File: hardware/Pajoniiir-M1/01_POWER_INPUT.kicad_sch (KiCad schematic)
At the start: 0 parts

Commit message: hardware: capture Rev A input eFuse schematic
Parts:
- added C1, C6: 100nF, Capacitor_SMD:C_0603_1608Metric, symbol Device:C
- added C2: 10uF, Capacitor_SMD:C_0805_2012Metric, symbol Device:C
- added C3, C8: 330uF_BULK_TUNING, symbol Device:C
- added C4, C5: 4.7nF, Capacitor_SMD:C_0603_1608Metric, symbol Device:C
- added C7: 22uF, Capacitor_SMD:C_1206_3216Metric, symbol Device:C
- added D1: 5V_TVS_TBD, symbol Device:D_TVS
- added J1: 5V_LOCKING_INPUT_TBD, symbol Connector_Generic:Conn_01x02
- added R1: 402k 1%, Resistor_SMD:R_0603_1608Metric, symbol Device:R_US
- added R2, R4: 150k 1%, Resistor_SMD:R_0603_1608Metric, symbol Device:R_US
- added R3: 562k 1%, Resistor_SMD:R_0603_1608Metric, symbol Device:R_US
- added R5: 750R 1%, Resistor_SMD:R_0603_1608Metric, symbol Device:R_US
- added R6: 10k PG PULLUP, Resistor_SMD:R_0603_1608Metric, symbol Device:R_US
- added U1: TPS259474ARPWR, symbol Pajoniiir-M1:TPS259474ARPWR
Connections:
- new net 3V3_SYS: R6.1
- new net 5V_SYS: C6.1, C7.1, C8.1, U1.6 (OUT)
- new net EFUSE_DVDT: C5.1, U1.7 (dVdt)
- new net EFUSE_EN_UVLO: R1.2, R2.1, U1.1 (EN_UVLO)
- new net EFUSE_ILM: R5.1, U1.9 (ILM)
- new net EFUSE_ITIMER: C4.1, U1.10 (ITIMER)
- new net EFUSE_OVLO: R3.2, R4.1, U1.2 (OVLO)
- new net EFUSE_PG: R6.2, U1.3 (PG)
- new net EFUSE_PGTH_TBD: U1.4 (PGTH)
- new net GND: C1.2, C2.2, C3.2, C4.2, C5.2, C6.2, C7.2, C8.2, D1.2 (A2), J1.2 (Pin_2), R2.2, R4.2, R5.2, U1.8 (GND)
- new net VIN_5V: C1.1, C2.1, C3.1, D1.1 (A1), J1.1 (Pin_1), R1.1, R3.1, U1.5 (IN)
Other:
- note added: "J1 and D1 exact MPN/footprints remain TBD-MECH/TBD-SURGE. Bulk 220/330/470uF is EVT tuning."
- note added: "PGTH NETWORK TBD-VALIDATE — do not populate blindly before threshold/timing review"
- note added: "Rev A targets: UVLO≈4.42V, OVLO≈5.70V, ILIM≈4.45A typ, ITIMER≈3.9ms, 5V rise≈11.8ms"

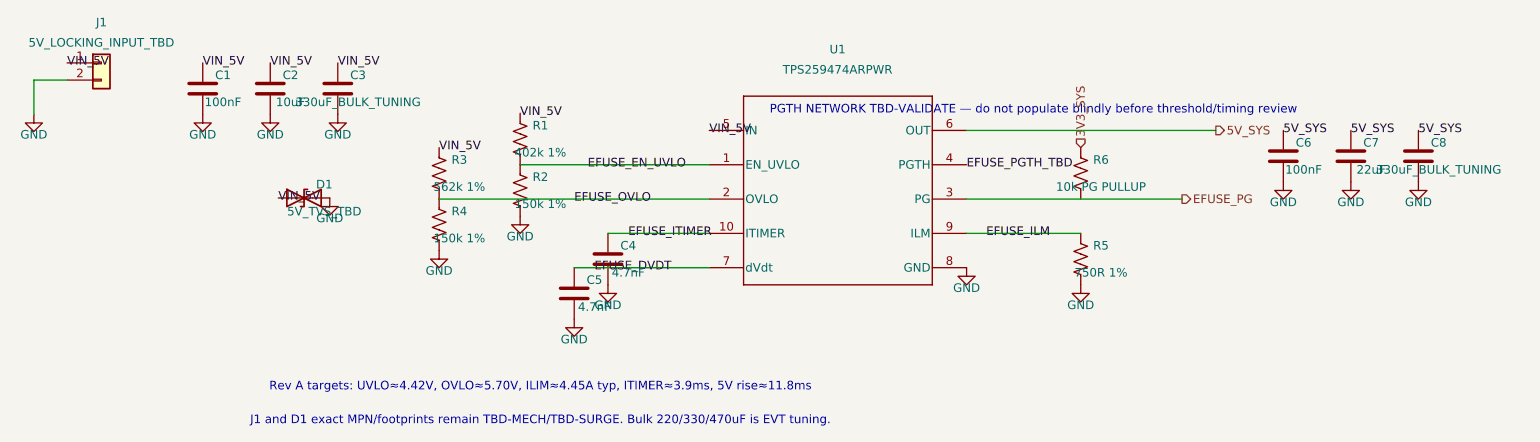
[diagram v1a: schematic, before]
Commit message: hardware: expose pre-shunt 5V protected rail
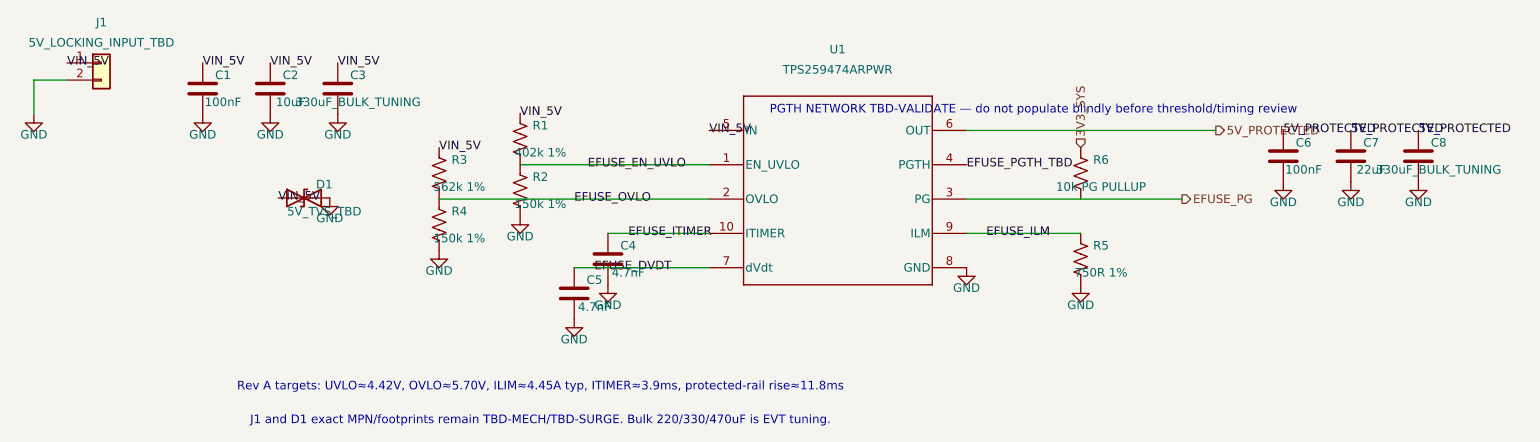
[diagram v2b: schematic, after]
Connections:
- net 5V_SYS renamed 5V_PROTECTED
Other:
- note added: "Rev A targets: UVLO≈4.42V, OVLO≈5.70V, ILIM≈4.45A typ, ITIMER≈3.9ms, protected-rail rise≈11.8ms"
- note removed: "Rev A targets: UVLO≈4.42V, OVLO≈5.70V, ILIM≈4.45A typ, ITIMER≈3.9ms, 5V rise≈11.8ms"
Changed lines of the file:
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@@
     (rev "A / M1-SCH-A")
     (company "Pajoniiir")
-    (comment 1 "TPS259474ARPWR input protection and 5V_SYS generation")
+    (comment 1 "TPS259474ARPWR input protection and 5V_PROTECTED generation")
     (comment 2 "PGTH intentionally TBD-VALIDATE")
   )
@@
     (stroke (width 0) (type default))
   )
-  (hierarchical_label "5V_SYS"
+  (hierarchical_label "5V_PROTECTED"
     (shape output)
     (at 195 50 0)
@@
     )
   )
-  (label "5V_SYS" (at 205 50 0)
+  (label "5V_PROTECTED" (at 205 50 0)
     (effects (font (size 1.27 1.27)))
   )
@@
     )
   )
-  (label "5V_SYS" (at 215 50 0)
+  (label "5V_PROTECTED" (at 215 50 0)
     (effects (font (size 1.27 1.27)))
   )
@@
     )
   )
-  (label "5V_SYS" (at 225 50 0)
+  (label "5V_PROTECTED" (at 225 50 0)
     (effects (font (size 1.27 1.27)))
   )
@@
     )
   )
-  (text "Rev A targets: UVLO≈4.42V, OVLO≈5.70V, ILIM≈4.45A typ, ITIMER≈3.9ms, 5V rise≈11.8ms"
+  (text "Rev A targets: UVLO≈4.42V, OVLO≈5.70V, ILIM≈4.45A typ, ITIMER≈3.9ms, protected-rail rise≈11.8ms"
     (exclude_from_sim no)
     (at 95 88 0)

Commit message: hardware: assign unique U7 reference to input eFuse
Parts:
- renumbered U1 to U7
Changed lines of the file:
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@@
     (dnp no)
     (fields_autoplaced yes)
-    (property "Reference" "U1" (at 139 38 0)
+    (property "Reference" "U7" (at 139 38 0)
       (effects (font (size 1.27 1.27)))
     )
@@
     (instances
       (project "Pajoniiir-M1"
-        (path "/2c8dd352-b7b8-4d9e-8f93-5dd43be2a100/31000001-6b2a-4a3a-8c91-000000000001" (reference "U1") (unit 1))
+        (path "/2c8dd352-b7b8-4d9e-8f93-5dd43be2a100/31000001-6b2a-4a3a-8c91-000000000001" (reference "U7") (unit 1))
       )
     )

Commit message: hardware: freeze TI RPW0010A eFuse footprint
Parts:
- U7: footprint (none) -> Pajoniiir-M1:Texas_RPW0010A_VQFN-HR-10_2x2mm
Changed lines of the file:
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@@
       (effects (font (size 1.27 1.27)))
     )
-    (property "Footprint" "" (at 120 50 0)
+    (property "Footprint" "Pajoniiir-M1:Texas_RPW0010A_VQFN-HR-10_2x2mm" (at 120 50 0)
       (effects (font (size 1.27 1.27)) (hide yes))
     )
